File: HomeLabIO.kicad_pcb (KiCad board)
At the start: 4 copper layers, 230 x 42 mm, 99 parts, among them J1 104031-0811, J2 HDMI_A, J3 Bus_M.2_Socket_M, J4 Conn_02x04_Odd_Even, J5 61900419521, J6 USB_C_Receptacle_USB2.0_16P, M2 CM4-GPIO, U1 MagJack-A70-112-331N126, U11 EMC2301, U13 TPD4EUSB30, U2 TPD4EUSB30, U3 TPD4EUSB30, U4 RT9742GGJ5, U5 74LVC1G07SE-7, U6 CP2102N-A02-GQFN24R, U7 AG5405, U8 AP3441SHE-7B, U9 SLB9672XU20FW1612XTMA1

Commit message: feat: add models
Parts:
- removed the G*** at (76.5, 80.5)

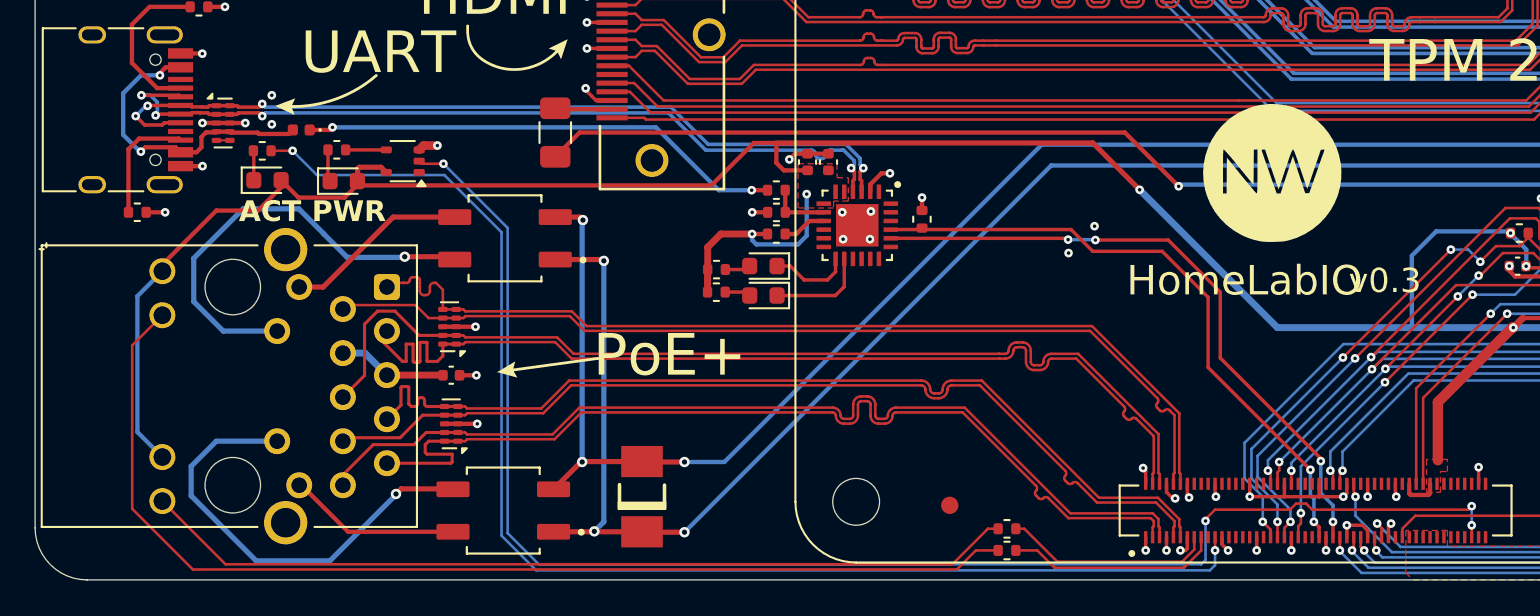
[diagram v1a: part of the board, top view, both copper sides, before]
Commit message: feat: update logo and move to back
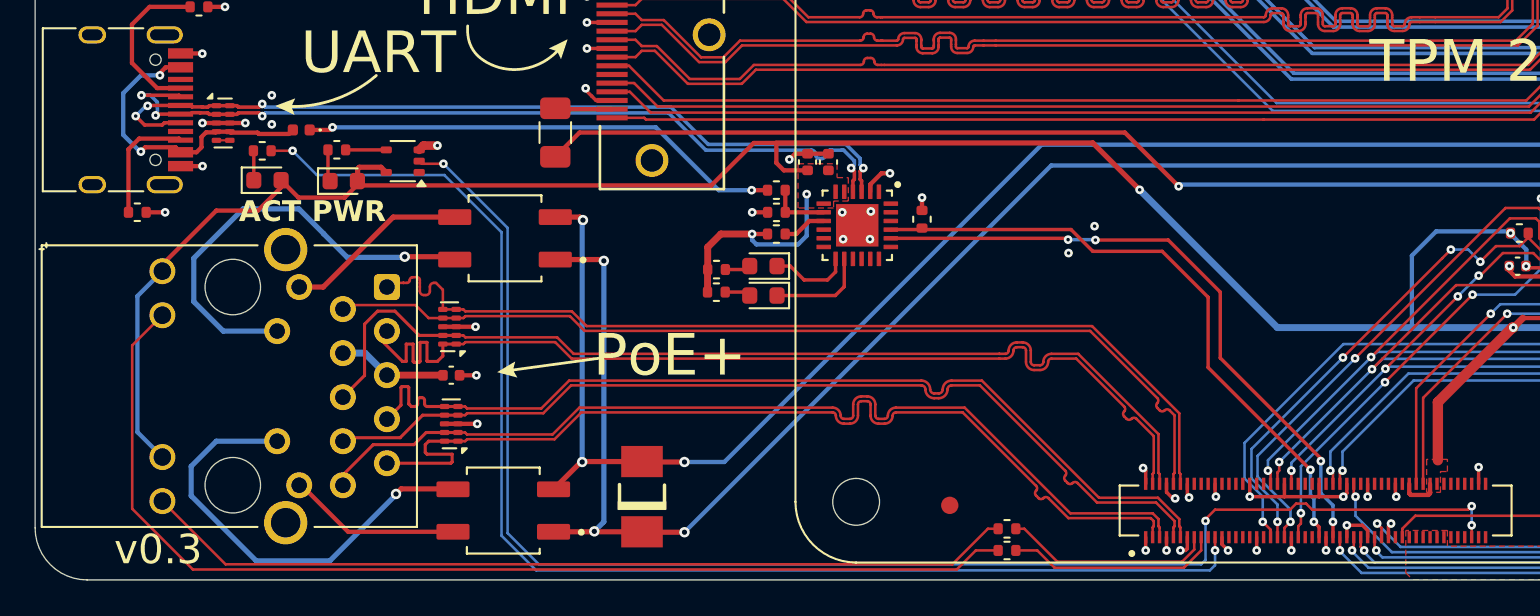
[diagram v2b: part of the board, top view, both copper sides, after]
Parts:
- G***: moved to B.Cu
- moved G*** 0.30 mm to (95.6, 82.8), turned to 180 degrees

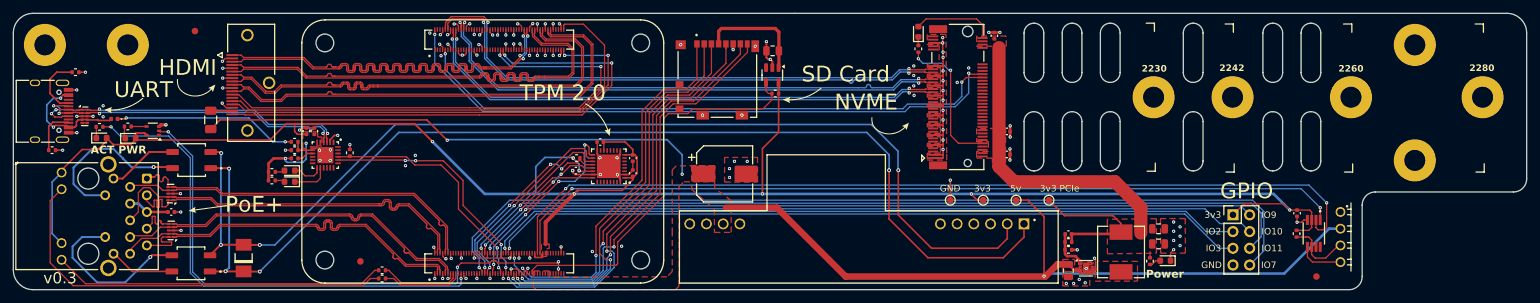
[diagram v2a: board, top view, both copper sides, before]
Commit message: fix: TPM pin connections
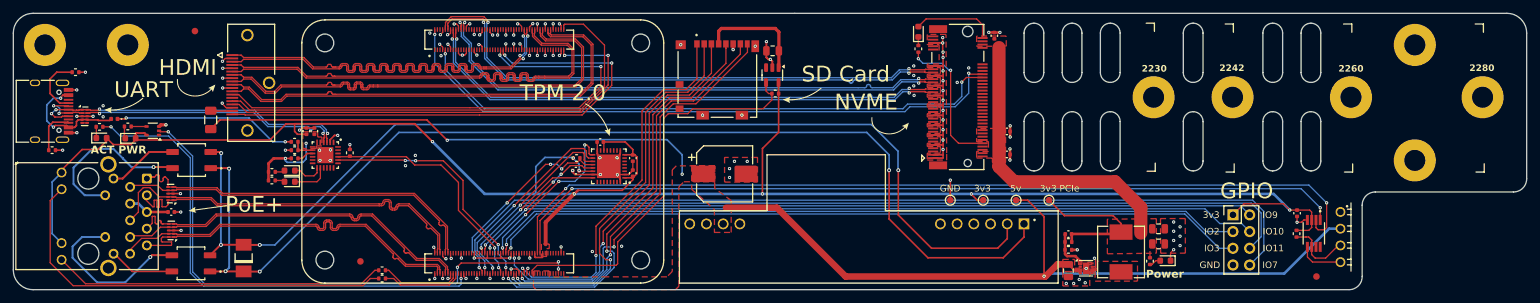
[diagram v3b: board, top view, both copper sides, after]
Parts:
- added G***: LOGO, HomeLabIO:QR-Code, B.Cu at (78.1, 95.0)
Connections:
- J4 pad 8: /CM4_GPIO/GPIO7 -> /CM4_GPIO/GPIO8
- M2 pad 37: /CM4_GPIO/GPIO7 -> /CM4_GPIO/TPM.CS
- M2 pad 39: /CM4_GPIO/TPM.CS -> /CM4_GPIO/GPIO8
- M2 pad 41: /CM4_GPIO/TPM.IRQ -> unconnected-(M2-GPIO25-Pad41)
- M2 pad 45: /CM4_GPIO/TPM.RST -> /CM4_GPIO/TPM.IRQ
- M2 pad 54: unconnected-(M2-GPIO4-Pad54) -> /CM4_GPIO/TPM.RST
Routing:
- net /CM4_GPIO/GPIO7: track 138.5 -> 0.00 mm, vias 1 -> 0
- net /CM4_GPIO/GPIO8: track 0.00 -> 137.9 mm, vias 0 -> 1
- net /CM4_GPIO/TPM.RST: track 29.2 -> 25.6 mm
- net /CM4_GPIO/TPM.CS: track 29.9 -> 30.5 mm

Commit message: feat: update silkscreen
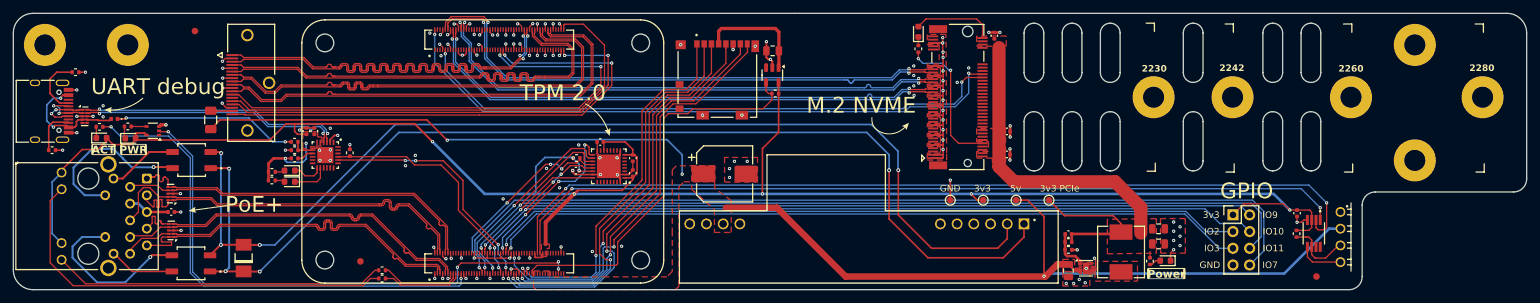
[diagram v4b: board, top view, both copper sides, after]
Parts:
- removed the G*** at (144.1, 77.0)
- removed the G*** at (52.0, 76.0)
- added S1: OSHW-Symbol_6.7x6mm_SilkScreen, Symbol:OSHW-Symbol_6.7x6mm_SilkScreen, B.Cu at (71.3, 88.0)
- added S2: WEEE-Logo_5.6x8mm_SilkScreen, Symbol:WEEE-Logo_5.6x8mm_SilkScreen, B.Cu at (221.0, 101.4)
- moved G*** 6.85 mm to (71.2, 95.2)
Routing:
- net GND: vias 134 -> 139
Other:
- board text added: "M.2 NVME"
- board text added: "UART debug"
- board text removed: "HDMI"
- board text removed: "NVME"
- board text removed: "SD Card"
- board text removed: "UART"
